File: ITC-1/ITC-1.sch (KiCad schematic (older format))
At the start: 78 parts, among them K1 кнопка, K2 кнопка, X1 крепеж, X2 крепеж, X3 крепеж, X4 крепеж

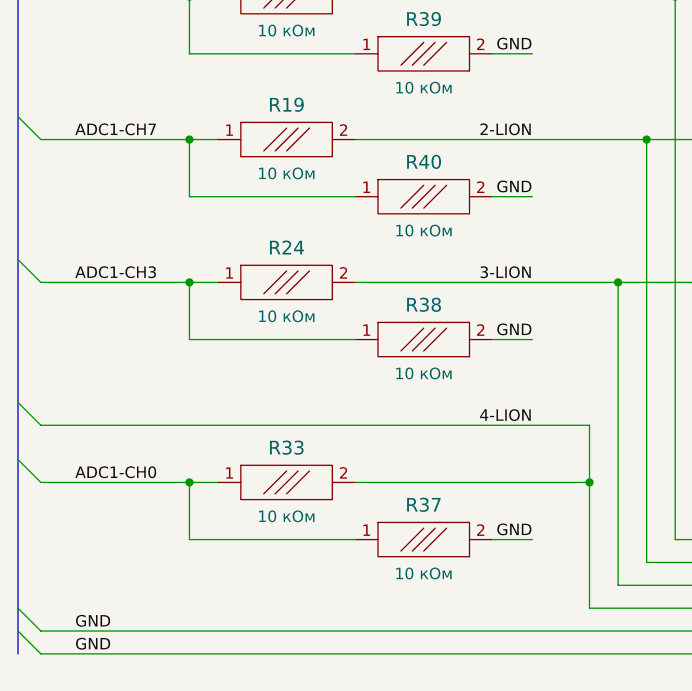
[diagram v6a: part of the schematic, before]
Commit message: определены номиналы делителей, добавлены ссылки на чип и дип
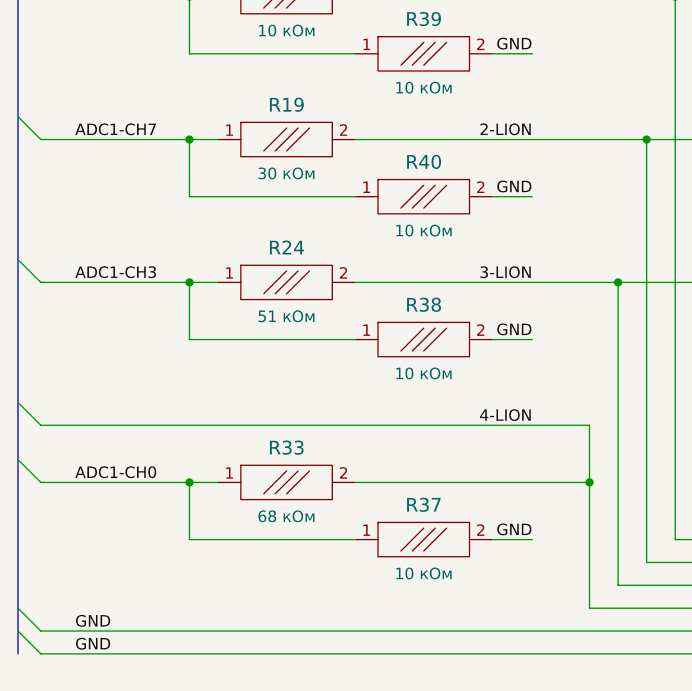
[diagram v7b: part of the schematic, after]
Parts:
- A1: LINK (none) -> не заказывал, есть в наличии
- C1, C4, C5, C6: LINK (none) -> https://www.chipdip.ru/product/grm188r71e105ka12d
- C2, C3: LINK (none) -> https://www.chipdip.ru/product/grm188r60j106me47d
- D1, D2, X1, X2, X3, X4: LINK (none) -> pcb element
- G1: LINK (none) -> https://www.chipdip.ru/product/lm1117gs-3.3
- HL1, HL2, HL3, HL4, HL5, HL6, HL7, HL8, HL9: LINK (none) -> https://www.chipdip.ru/product/kpb-3025surkcgkc
- K1, K2: LINK (none) -> https://www.chipdip.ru/product/tyco-1437566-3-fsmsm
- R1, R15, R16, R2, R20, R23, R26, R27, R28, R32, R37, R38, R39, R40, R41, R42, R5, R6, R7, R8, R9: LINK (none) -> https://www.chipdip.ru/product0/65097
- R10, R11, R12, R13, R14, R17, R18, R21, R22, R3, R4: LINK (none) -> https://www.chipdip.ru/product0/654254294
- R19: LINK (none) -> https://www.chipdip.ru/product0/20824; Номинал 10 кОм -> 30 кОм
- R24: LINK (none) -> https://www.chipdip.ru/product0/469851073; Номинал 10 кОм -> 51 кОм
- R29: LINK (none) -> https://www.chipdip.ru/product0/10149
- R33: LINK (none) -> https://www.chipdip.ru/product0/36049; Номинал 10 кОм -> 68 кОм
- VD1: LINK (none) -> https://www.chipdip.ru/product/smbj18a
- VT1, VT2: LINK (none) -> https://www.chipdip.ru/product/irlml2246trpbf
- VT10, VT11, VT3, VT4, VT5, VT6, VT7, VT8, VT9: LINK (none) -> https://www.chipdip.ru/product/irlml6344trpbf
- VT13: LINK (none) -> https://www.chipdip.ru/product/pbss4540z.115
- XP4, XP5: LINK (none) -> не заказана, есть в наличии

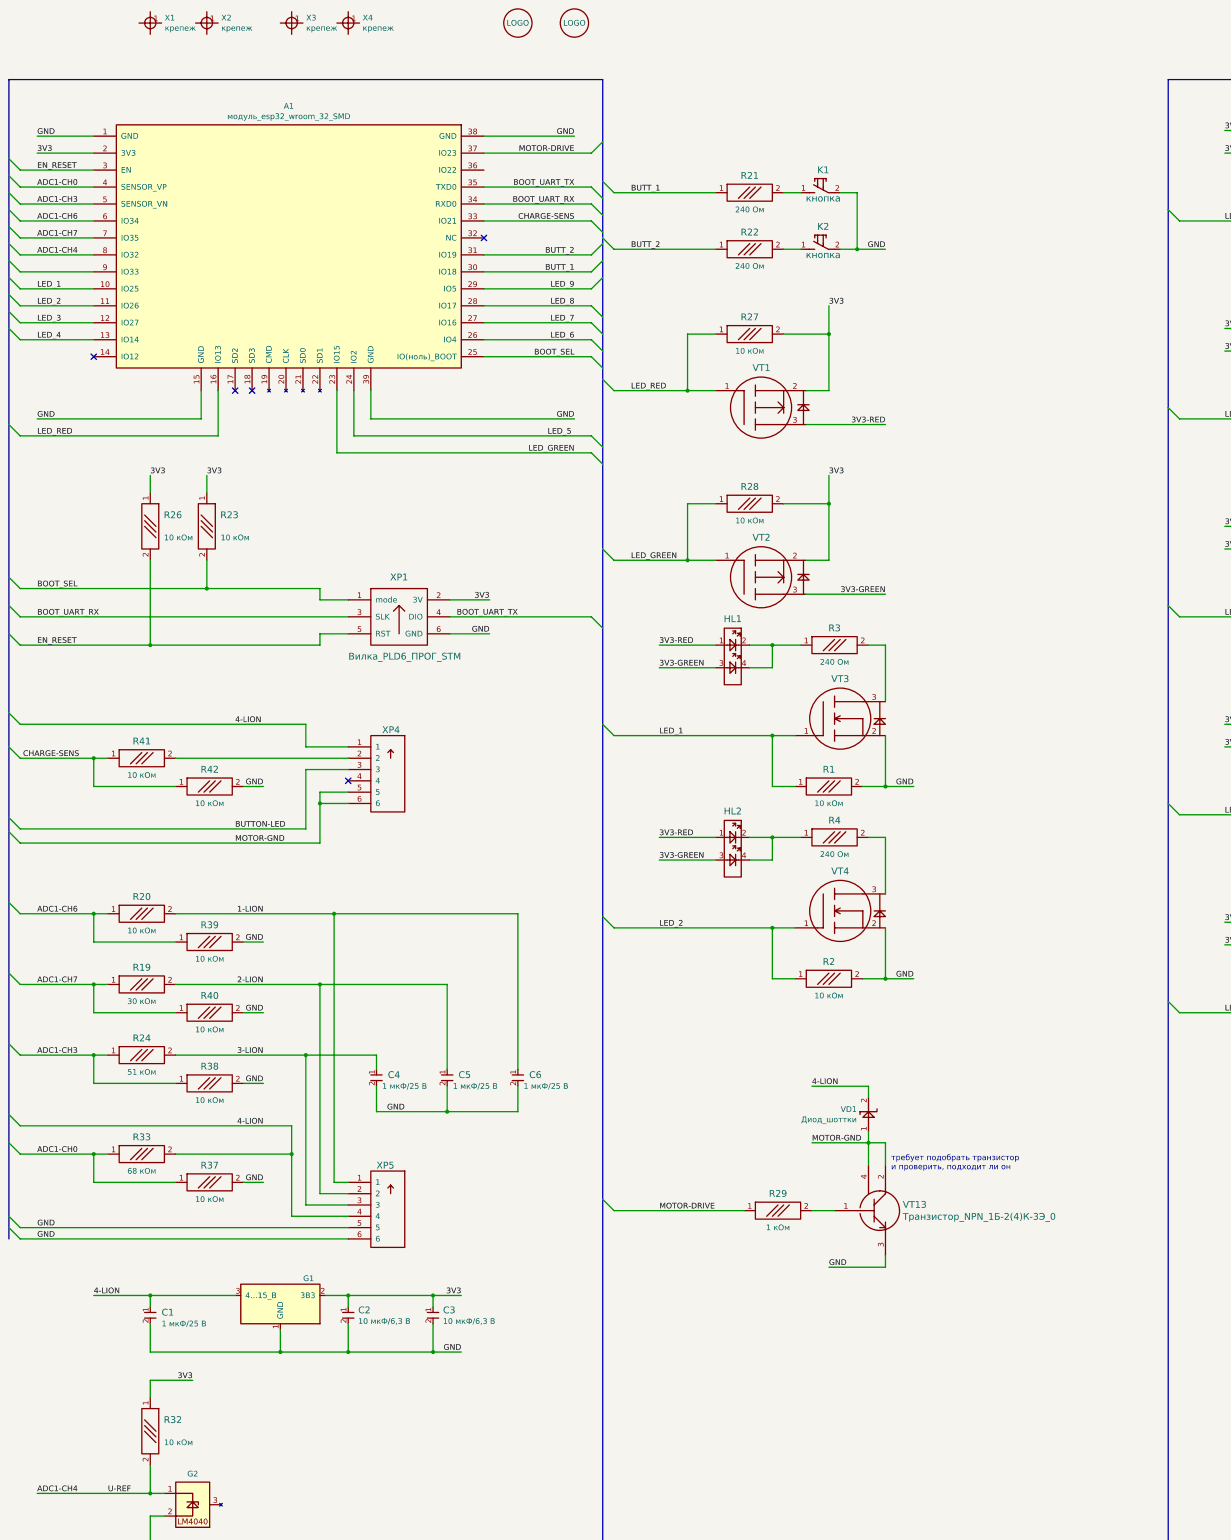
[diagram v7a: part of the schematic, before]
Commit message: PCB: транзистор N-канал, утолщены дорожки, кнопка BOOT, заменен прог.
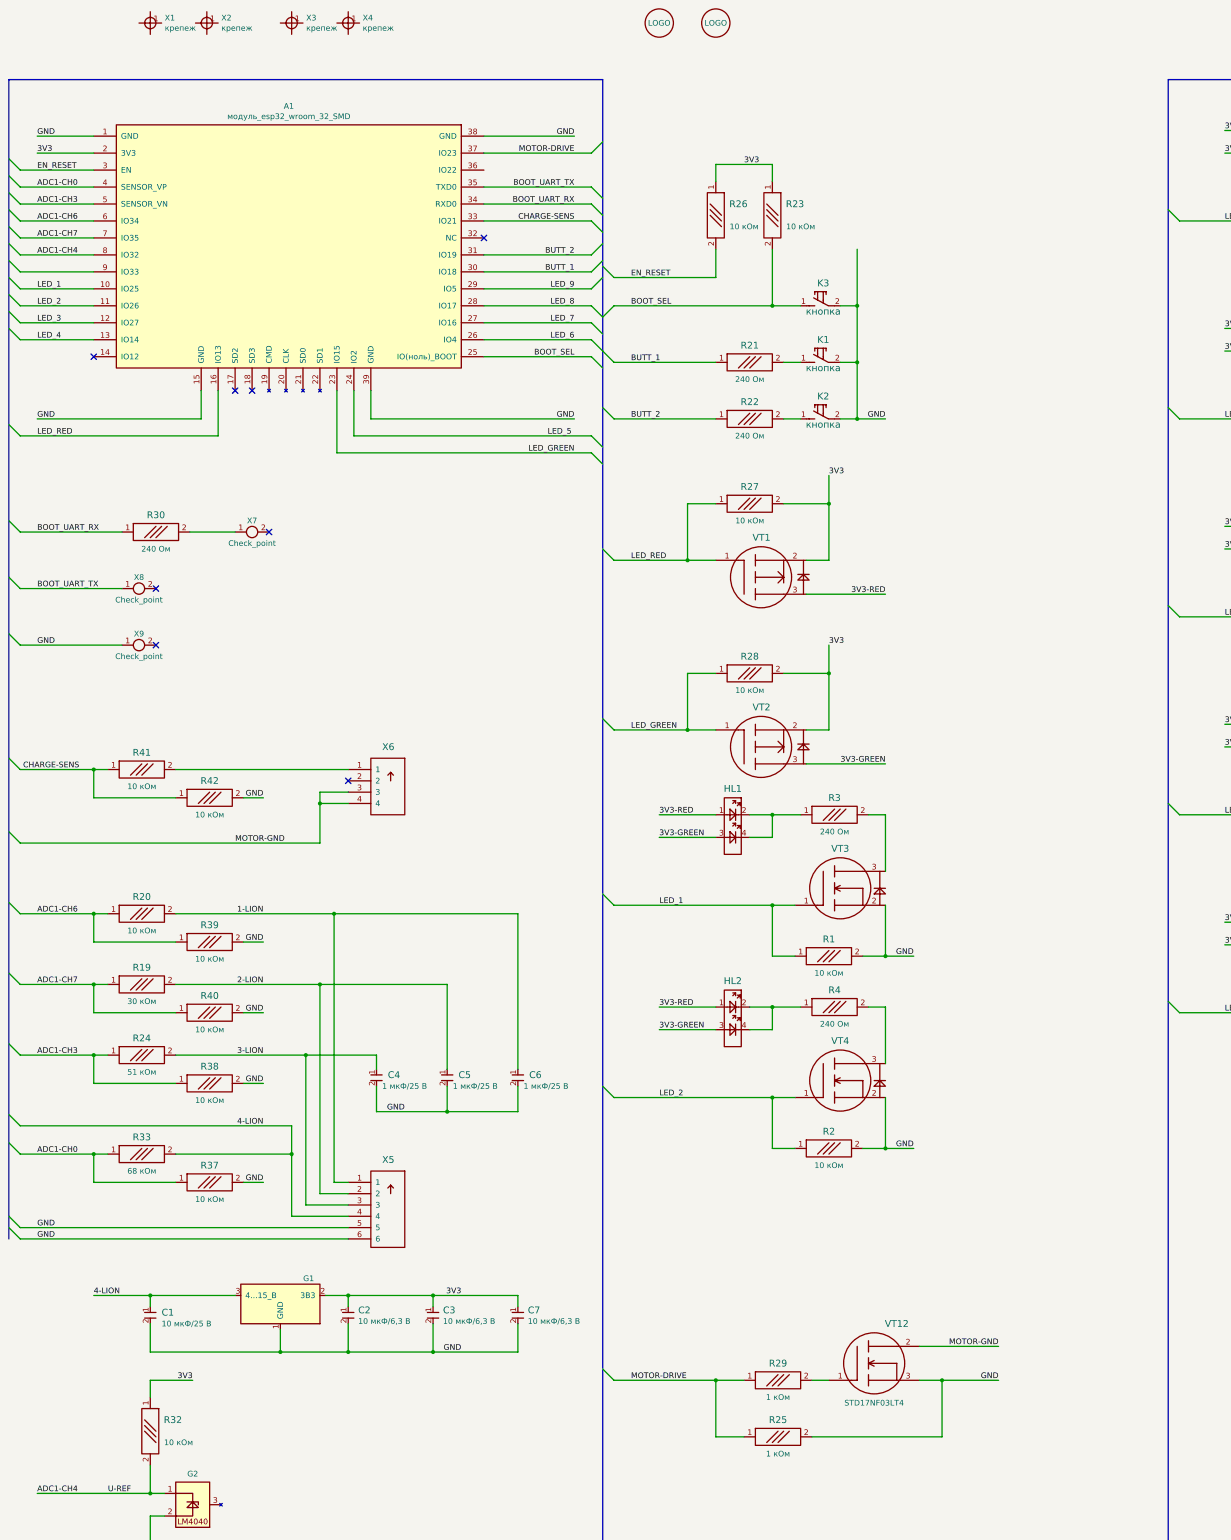
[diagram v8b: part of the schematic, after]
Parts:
- removed VD1: Диод_шоттки, N_VD_HL:Диод_SMB_pnp, symbol elements:Диод_шоттки
- removed VT13: Транзистор_NPN_1Б-2(4)К-3Э_0, N_VD_HL:Транзистор_NPN_SOT223_pnp, symbol elements:Транзистор_NPN_1Б-2(4)К-3Э_0
- removed XP1: Вилка_PLD6_ПРОГ_STM, N_X:Вилка_PLLD6_угловая_вертикальная, symbol elements:Вилка_PLD6_ПРОГ_STM
- removed XP4: Вилка_PLS6, N_X:Вилка_PLD6_вертикальная, symbol elements:Вилка_PLS6
- added C7: Конденсатор_керамический, N_RLC:Конденсатор_SMD_0603_pnp, symbol elements:Конденсатор_керамический
- added K3: кнопка, N_X:Кнопка_FSMSM, symbol elements:кнопка
- added R25, R30: Резистор_0,065Вт, N_RLC:Резистор_SMD_0603_0,065_Вт_pnp, symbol elements:Резистор_0,065Вт
- added VT12: Транзистор_полевой_N-канал, N_VD_HL:Транзистор_N-канал_dpak_DS, symbol elements:Транзистор_полевой_N-канал
- added X6: Вилка_PLS4, N_X:Вилка_PLD4_вертикальная, symbol elements:Вилка_PLS4
- added X7, X8, X9: Check_point, N_X:Пробник, symbol elements_2020:Check_point
- C1: footprint N_RLC:Конденсатор_SMD_0603_pnp -> N_RLC:Конденсатор_SMD_IEC_0805; Номинал 1 мкФ/25 В -> 10 мкФ/25 В
- renumbered XP5 to X5
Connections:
- net 3V3: now also C7.1
- net BOOT_SEL: now also K3.1
- net BOOT_UART_RX: now also R30.1
- net BOOT_UART_TX: now also X8.1
- net GND: now also C7.2, K3.2, R25.2, VT12.3, X9.1
- net MOTOR-DRIVE: now also R25.1
- net MOTOR-GND: now also VT12.2, X6.3, X6.4
- net at R41.2: now also X6.1
- net at R29.2: now also VT12.1
- new net: R30.2, X7.1
- no-connect marks 5 -> 8
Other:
- note removed: "требует подобрать транзистор \nи проверить, подходит ли он"
- moved on the sheet: HL1, HL2, K1, K2, R1, R2, R21, R22, R23, R26, R27, R28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
